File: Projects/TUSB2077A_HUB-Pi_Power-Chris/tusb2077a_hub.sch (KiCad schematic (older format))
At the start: 2 parts

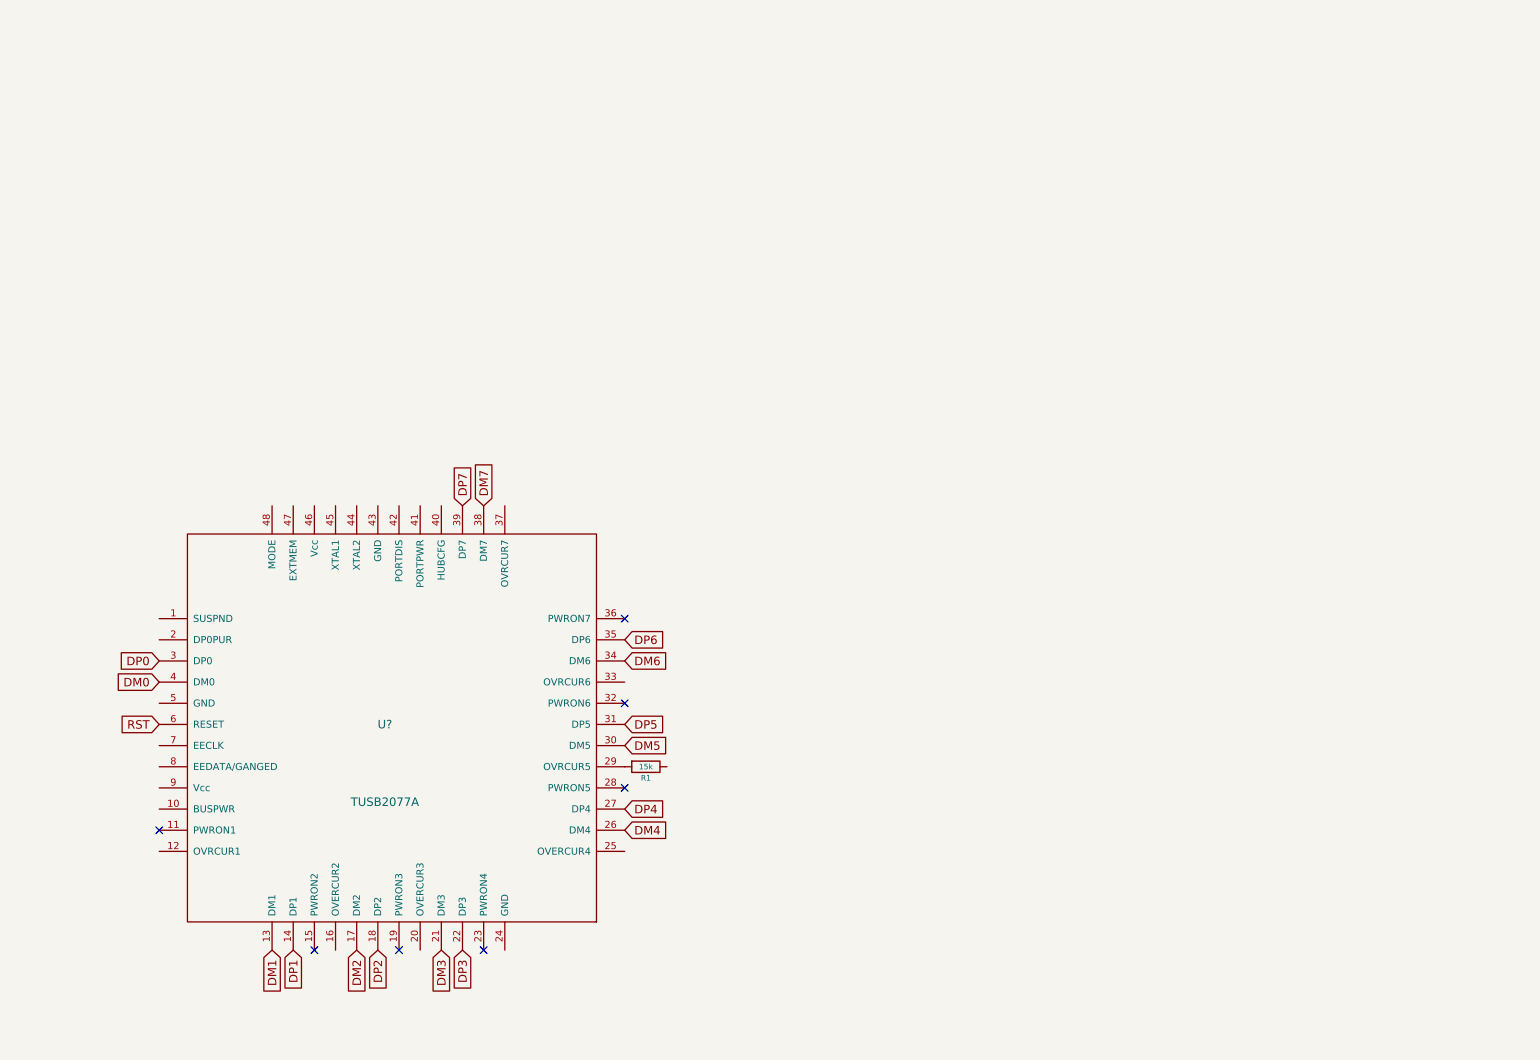
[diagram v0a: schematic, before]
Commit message: Added on to Schematic
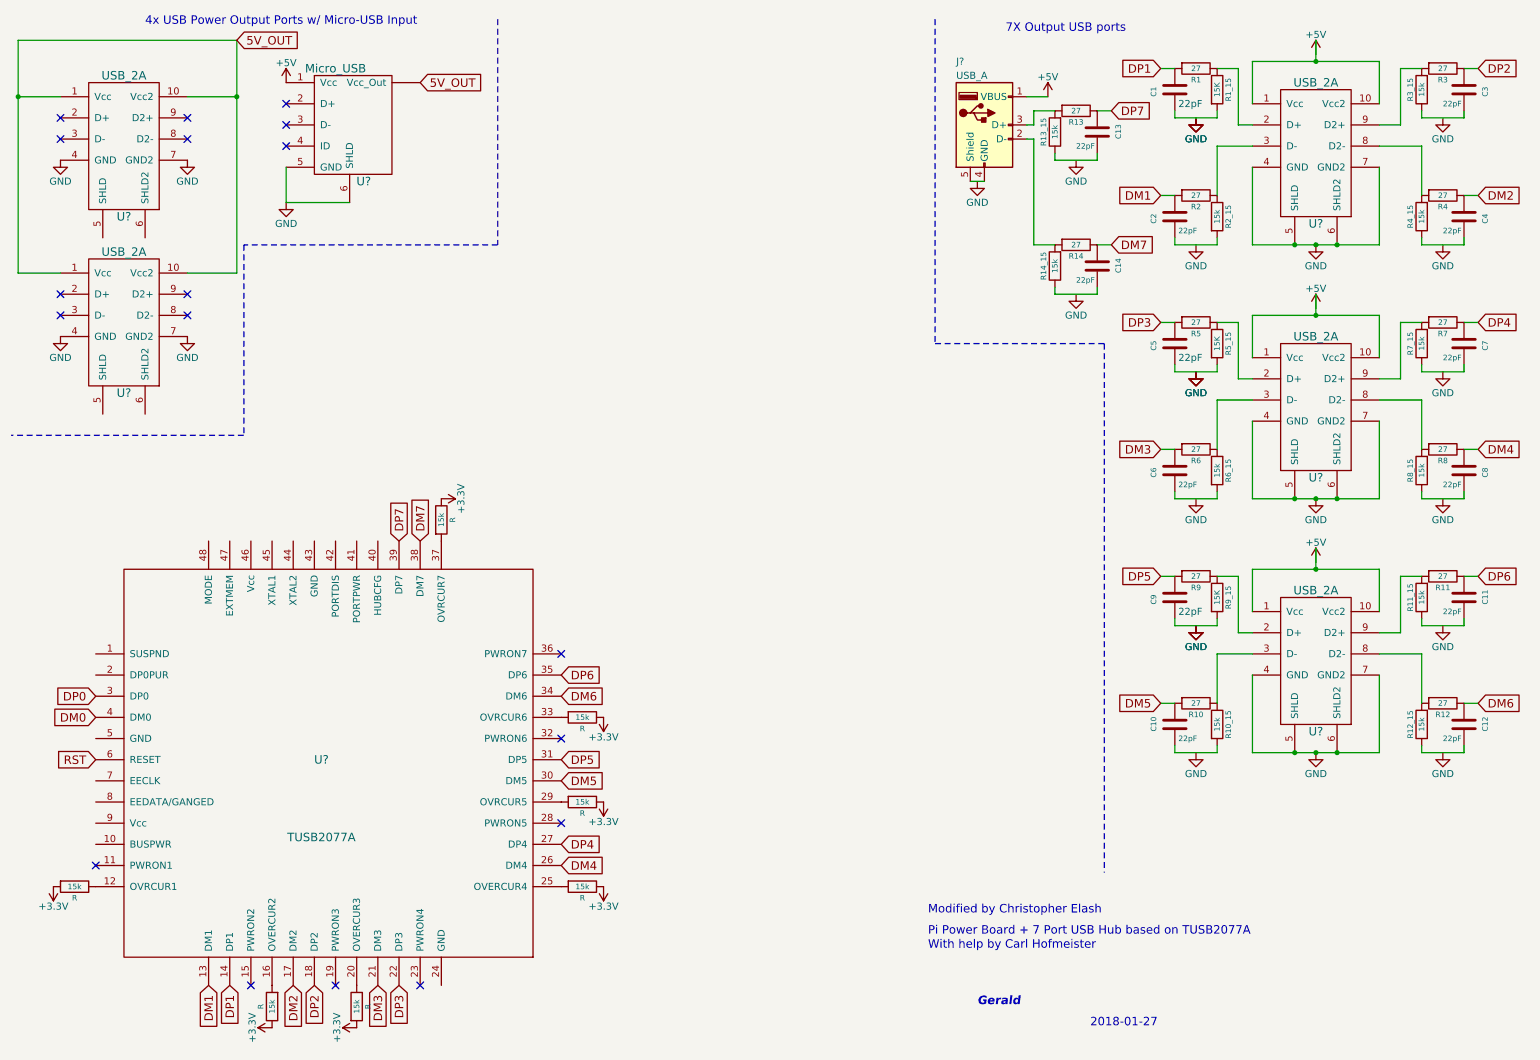
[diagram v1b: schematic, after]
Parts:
- added C1, C10, C11, C12, C13, C14, C2, C3, C4, C5, C6, C7, C8, C9: 22pF, symbol C
- added J?: USB_A, symbol USB_A
- added R (x6), R10_15, R11_15, R12_15, R13_15, R14_15, R2_15, R3_15, R4_15, R6_15, R7_15, R8_15: 15k, symbol R
- added R1, R10, R11, R12, R13, R14, R2, R3, R4, R5, R6, R7, R8, R9: 27, symbol R
- added R1_15, R5_15, R9_15: 15K, symbol R
- added U? (x5): USB_2A, symbol USB_2A
- added U?: Micro_USB, symbol Micro_USB
- renumbered R1 to R
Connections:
- net DM1: now also C2.1, R2.2
- net DM2: now also C4.1, R4.1
- net DM3: now also C6.1, R6.2
- net DM4: now also C8.1, R8.1
- net DM5: now also C10.1, R10.2
- net DM6: now also C12.1, R12.1
- net DM7: now also C14.1, R14.1
- net DP1: now also C1.1, R1.2
- net DP2: now also C3.1, R3.1
- net DP3: now also C5.1, R5.2
- net DP4: now also C7.1, R7.1
- net DP5: now also C9.1, R9.2
- net DP6: now also C11.1, R11.1
- net DP7: now also C13.1, R13.1
- net at U?.12 (OVRCUR1): now also R.1
- net at U?.16 (OVERCUR2): now also R.2
- net at U?.20 (OVERCUR3): now also R.1
- net at U?.25 (OVERCUR4): now also R.2
- net at U?.33 (OVRCUR6): now also R.2
- net at U?.37 (OVRCUR7): now also R.2
- net +3V3: now reaches R.1
- net +3V3: now also R.1, R.1, R.1, R.1, R.2, R.2
- new net: U?.1 (Vcc), U?.10 (Vcc2) (x3)
- new net: R1.1, R1_15.1, U?.2 (D+)
- new net: R2.1, R2_15.1, U?.3 (D-)
- new net: R4.2, R4_15.2, U?.8 (D2-)
- new net: R3.2, R3_15.2, U?.9 (D2+)
- new net: C1.2, R1_15.2
- new net: C2.2, R2_15.2
- new net: C3.2, R3_15.1
- new net: C4.2, R4_15.1
- new net: R5.1, R5_15.1, U?.2 (D+)
- new net: R6.1, R6_15.1, U?.3 (D-)
- new net: R8.2, R8_15.2, U?.8 (D2-)
- new net: R7.2, R7_15.2, U?.9 (D2+)
- new net: C5.2, R5_15.2
- new net: C6.2, R6_15.2
- new net: C7.2, R7_15.1
- new net: C8.2, R8_15.1
- new net: R9.1, R9_15.1, U?.2 (D+)
- new net: R10.1, R10_15.1, U?.3 (D-)
- new net: R12.2, R12_15.2, U?.8 (D2-)
- new net: R11.2, R11_15.2, U?.9 (D2+)
- new net: C9.2, R9_15.2
- new net: C10.2, R10_15.2
- new net: C11.2, R11_15.1
- new net: C12.2, R12_15.1
- new net: J?.2 (D-), R14.2, R14_15.2
- new net: J?.3 (D+), R13.2, R13_15.2
- new net: J?.4 (GND), J?.5 (Shield)
- new net: C13.2, R13_15.1
- new net: C14.2, R14_15.1
- new net +5V: J?.1 (VBUS), U?.1 (Vcc)
- new net 5V_OUT: U?.1 (Vcc), U?.1 (Vcc), U?.10 (Vcc2), U?.10 (Vcc2), U?.~ (Vcc_Out)
- new net GND: U?.4 (GND), U?.4 (GND), U?.4 (GND), U?.4 (GND), U?.4 (GND), U?.5 (GND), U?.5 (SHLD), U?.5 (SHLD), U?.5 (SHLD), U?.6 (SHLD), U?.6 (SHLD2), U?.6 (SHLD2), U?.6 (SHLD2), U?.7 (GND2), U?.7 (GND2), U?.7 (GND2), U?.7 (GND2), U?.7 (GND2)
- no-connect marks 7 -> 18
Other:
- note added: "2018-01-27"
- note added: "4x USB Power Output Ports w/ Micro-USB Input"
- note added: "7X Output USB ports"
- note added: "Gerald"
- note added: "Modified by Christopher Elash"
- note added: "Pi Power Board + 7 Port USB Hub based on TUSB2077A"
- note added: "With help by Carl Hofmeister"
- moved on the sheet: R, U?

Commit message: added onto schematic
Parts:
- added C15, C16: 33pF, symbol C
- added C17: 1uF, symbol C
- added C18: 10uF, symbol C
- added D1, D2, D3, D4: LED, symbol LED
- added J1: Conn_01x02, symbol Conn_01x02
- added R15, R16, R17, R18: 1K, symbol R
- added R19: 1.5K, symbol R
- added U?: TPS76333, TO_SOT_Packages_SMD:SOT-23-5, symbol TPS76333
- added Y1: 6 MHz, symbol Crystal
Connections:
- net labels added: DPOPUR, HUBCFG, PORTDIS, PORTPWR, SUSPND, VCC
- wire segments 124 -> 155
- no-connect marks 18 -> 19
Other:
- note added: "OUT"
- note added: "Sensors"
- note added: "Voltage Regulator 3.3V"
